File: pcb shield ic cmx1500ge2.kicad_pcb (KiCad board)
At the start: 2 copper layers, 68.6 x 53.3 mm, 14 parts, among them P1 Power, P2 Analog, P3 Digital, P4 Digital, P5 CONN_01X01, P6 CONN_01X01, P7 CONN_01X01, P8 CONN_01X01

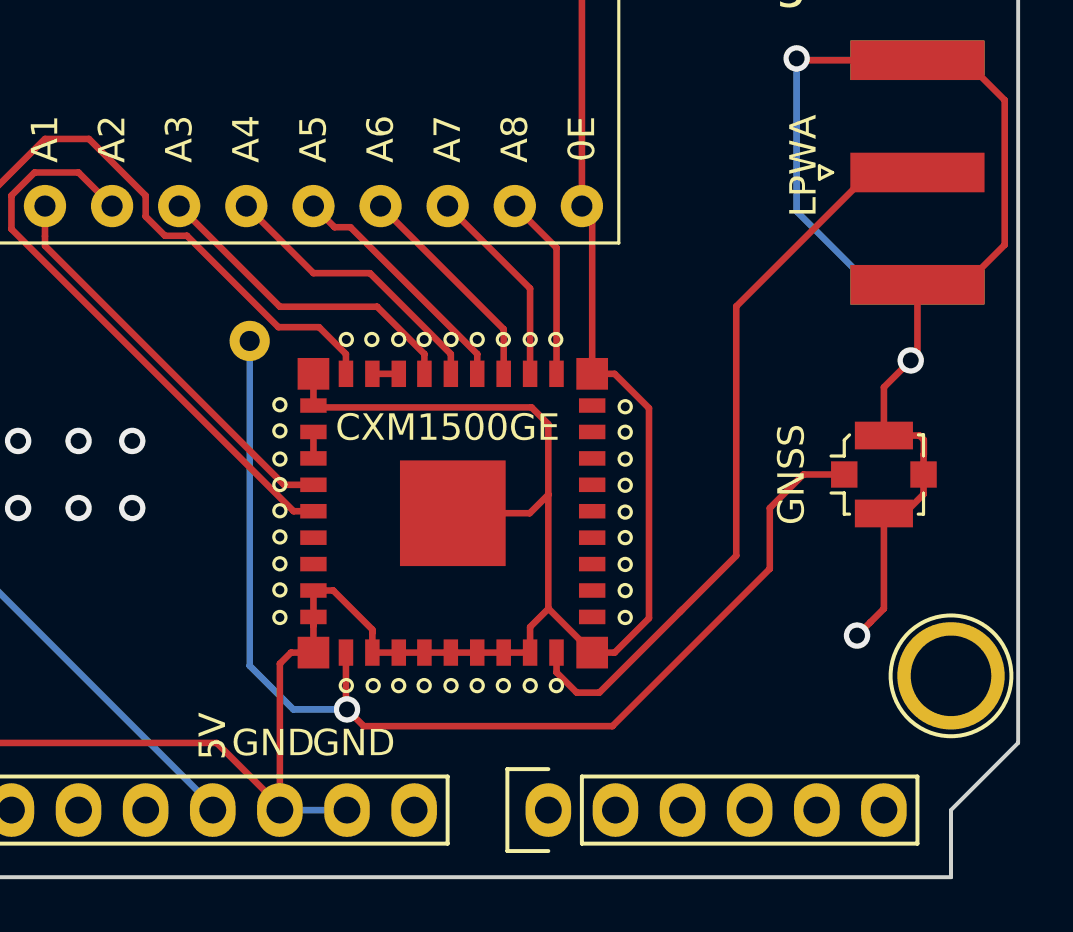
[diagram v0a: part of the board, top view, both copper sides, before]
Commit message: mengubah routing pada jalur sinyal rf agar impedasi 50 ohm dan menambah file duplicate print pcb
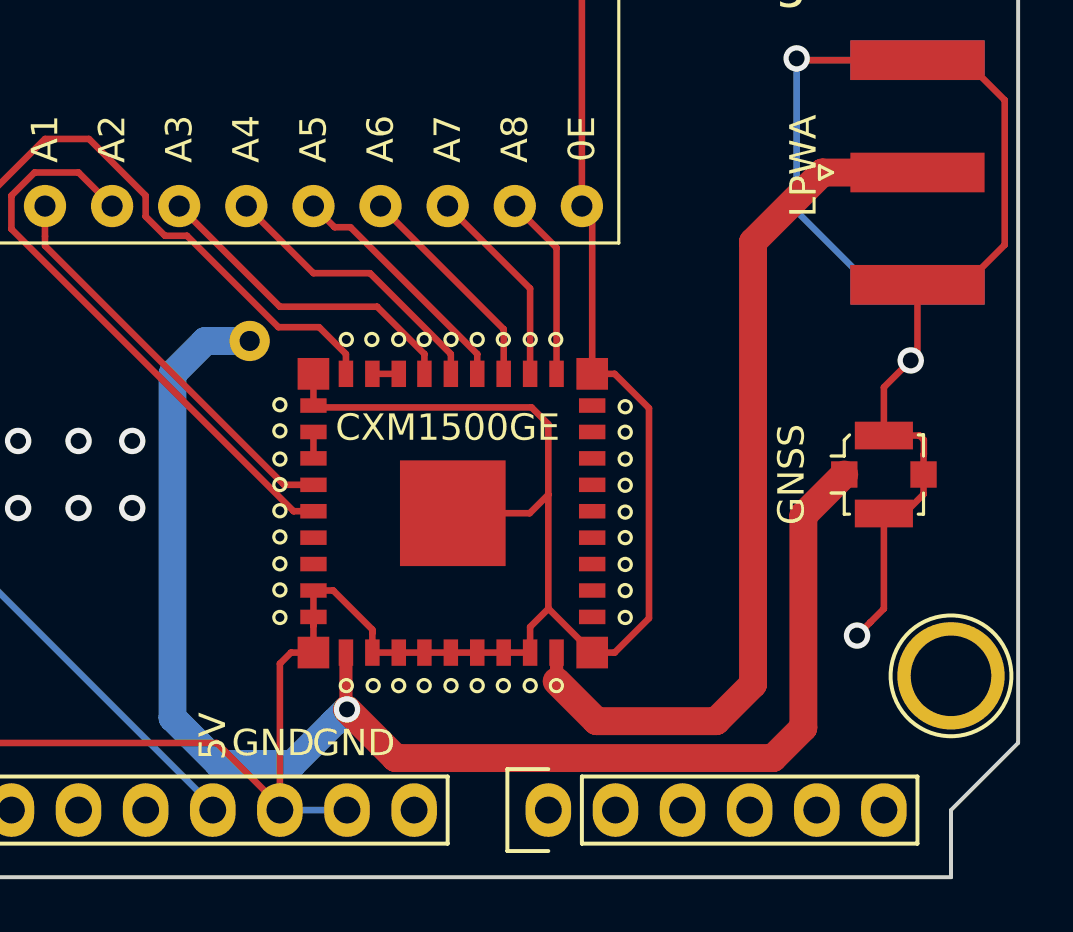
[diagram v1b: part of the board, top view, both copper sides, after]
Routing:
- net Net-(J1-Pad1): track 43.3 -> 55.6 mm
- net Net-(J2-Pad1): track 28.6 -> 33.8 mm
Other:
- net class rf added: clearance 0.2, trace_width 1.05736, via_dia 0.6, via_drill 0.4

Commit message: initial commit
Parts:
- removed CJMCU: modul_lvl-conveter_cjmcu, modul:modul_lvl_conveter_cjmcu
- removed CXM1500GE: CXM1500GE, modul:CXM1500GE
- removed GNSS: SMA, Connector_Coaxial:U.FL_Molex_MCRF_73412-0110_Vertical
- removed LM2596_1: modul_dc-dc_lm2596, modul:modul_lvl_dc-dc_lm2596
- removed LPWA: SMA, Connector_Coaxial:SMA_Amphenol_132289_EdgeMount
- removed P5, P6, P8: CONN_01X01, Socket_Arduino_Uno:Arduino_1pin
- removed push to: SWITCH-DPDT, Switches:Switch_DPDT_6p_TH
- added C1: 100uF, Capacitors:C_Ceramic_SMD_0603, F.Cu at (132.7, 116.7)
- added C2: 0.1u, Capacitors:C_Ceramic_SMD_0603, F.Cu at (113.3, 85.9)
- added C3: 0.1u, Capacitors:C_Ceramic_SMD_0603, F.Cu at (123.1, 103.4)
- added C4: 100uF, Capacitors:C_Ceramic_SMD_0603, F.Cu at (127.5, 116.7)
- added C5: 10uf, Capacitors:C_Ceramic_SMD_0603, F.Cu at (138.2, 116.7)
- added J1: SMA, Connectors_SMA:SMA_Male_Angled_TH, F.Cu at (151.9, 107.4)
- added J3: Conn_01x01_Male, Headers:Pin_Header_1x01_Male_10mil_Straight_TH, F.Cu at (120.0, 109.1)
- added J4: Conn_01x01_Male, Headers:Pin_Header_1x01_Male_10mil_Straight_TH, F.Cu at (113.6, 109.0)
- added R1: 121, Resistors:R_Chip_SMD_0603, F.Cu at (135.2, 110.9)
- added R2: ?, Resistors:R_Chip_SMD_0603, F.Cu at (129.8, 110.9)
- added R3: RES, Resistors:R_Chip_SMD_0603, F.Cu at (135.9, 87.8)
- added R4: RES, Resistors:R_Chip_SMD_0603, F.Cu at (143.9, 80.5)
- added R5: 10, Resistors:R_Chip_SMD_0603, F.Cu at (116.6, 89.6)
- added R6: 10, Resistors:R_Chip_SMD_0603, F.Cu at (120.2, 89.6)
- added R7: -, Resistors:R_Chip_SMD_0603, F.Cu at (122.3, 109.1)
- added R8: -, Resistors:R_Chip_SMD_0603, F.Cu at (115.9, 109.2)
- added REF**: AP2112, AP2112:AP2112, F.Cu at (143.8, 102.1)
- added RESET: BUTTON, Push_Buttons:Button_4p_W-6.0mm_L-6.0mm_Normal_SMD, F.Cu at (130.4, 93.7)
- added U1: CXM1501GE, modul:_CXM1501GE, F.Cu at (153.7, 98.3)
- added U2: TXS0108EPW, Package_SO:TSSOP-20_4.4x6.5mm_P0.65mm, F.Cu at (119.0, 96.2)
- added U3: LM1117-Adj, smd:TO261AA-LM1117_rev, F.Cu at (132.8, 103.9)
- P2: footprint Socket_Arduino_Uno:Socket_Strip_Arduino_1x06 -> Socket_Arduino_Uno:Socket_Strip_Arduino_1x08
- P7: value CONN_01X01 -> Communication; footprint Socket_Arduino_Uno:Arduino_1pin -> Socket_Arduino_Mega:Socket_Strip_Arduino_1x08
- moved P7 27.8 mm to (154.0, 75.6)
- moved P3 26.2 mm to (103.6, 75.6)
- moved P4 25.5 mm to (131.3, 75.6)
- moved P1 24.7 mm to (114.2, 123.8)
- moved P2 24.7 mm to (137.1, 123.8)
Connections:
- P1 pad 1: Net-(P1-Pad1) -> (no net)
- P1 pad 2: /IOREF -> (no net)
- P1 pad 3: /Reset -> (no net)
- P1 pad 4: +3V3 -> (no net)
- P1 pad 8: /Vin -> (no net)
- P2 pad 1: /A0 -> (no net)
- P2 pad 2: /A1 -> (no net)
- P2 pad 3: /A2 -> (no net)
- P2 pad 4: /A3 -> (no net)
- P2 pad 5: /A4(SDA) -> (no net)
- P2 pad 6: /A5(SCL) -> (no net)
- P3 pad 1: /A5(SCL)_l -> (no net)
- P3 pad 10: /8 -> (no net)
- P3 pad 2: /A4(SDA)_l -> (no net)
- P3 pad 3: /AREF -> (no net)
- P3 pad 5: /13(SCK) -> (no net)
- P3 pad 7: /11(**_MOSI) -> (no net)
- P3 pad 8: /10(**_SS) -> (no net)
- P4 pad 1: /7 -> (no net)
- P4 pad 2: /6(**) -> (no net)
- P4 pad 3: /5(**) -> (no net)
- P4 pad 6: /2 -> /19(Rx1)
- P4 pad 7: /1(Tx) -> (no net)
- P4 pad 8: /0(Rx) -> (no net)
- P7 pad 1: Net-(P7-Pad1) -> (no net)
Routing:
- net GND: track 231.6 -> 44.7 mm, vias 25 -> 46
- net /19(Rx1): track 0.00 -> 65.8 mm, vias 0 -> 1
- net /18(Tx1): track 0.00 -> 58.8 mm, vias 0 -> 1
- net /CTS_IC: track 0.00 -> 50.4 mm, vias 0 -> 4
- net /RTS_IC: track 0.00 -> 47.0 mm
- net /INT_1: track 0.00 -> 46.8 mm, vias 0 -> 4
- net Net-(J1-Pad1): track 55.6 -> 10.3 mm, vias 1 -> 0
- net /+2V: track 42.5 -> 86.7 mm, vias 0 -> 8
- net /TX_IC: track 0.00 -> 40.0 mm
- net /RX_IC: track 0.00 -> 35.1 mm
- net /ENB: track 0.00 -> 34.8 mm, vias 0 -> 5
- net /12(MISO): track 12.8 -> 41.7 mm, vias 0 -> 2
- net /9(**): track 13.6 -> 36.9 mm, vias 0 -> 3
- net Net-(TXS0108E-8_1-Pad3): track 21.8 -> 0.00 mm
- net /INT_2: track 0.00 -> 21.2 mm, vias 0 -> 1
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- removed copper zone on B.Cu, net GND
- removed copper zone on F.Cu, net GND
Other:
- board size 68.6 x 53.3 mm -> 73.2 x 53.3 mm
- net class Default: trace_width 0.25 -> 0.3
- net class power added: clearance 0.2, trace_width 0.5, via_dia 0.6, via_drill 0.4
- net class rf: clearance 0.2 -> 0.3; trace_width 1.05736 -> 1.44459
- net class small added: clearance 0.1, trace_width 0.3, via_dia 0.6, via_drill 0.4
- board text removed: "1"
- board text removed: "debag"
